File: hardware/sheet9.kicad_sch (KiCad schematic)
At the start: 0 parts

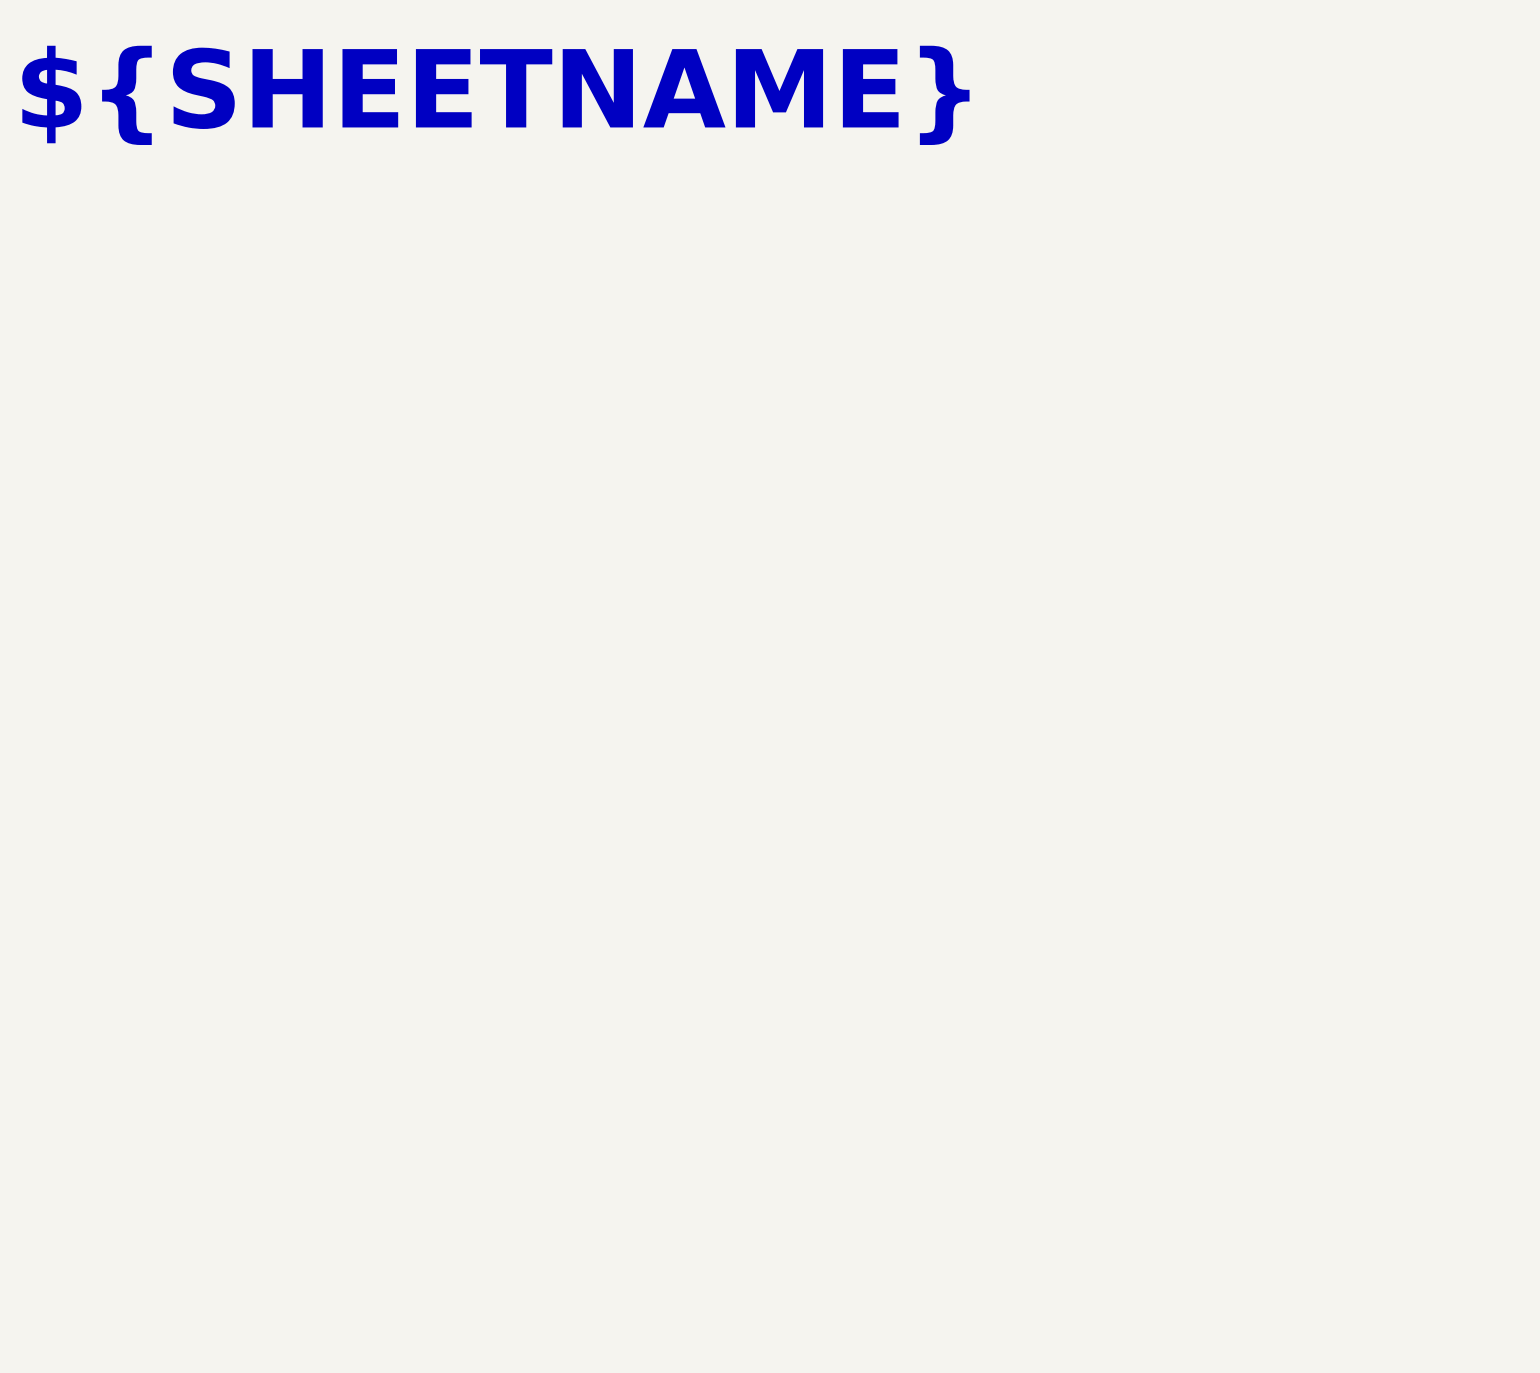
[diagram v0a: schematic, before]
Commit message: hardware(feat): add board layers
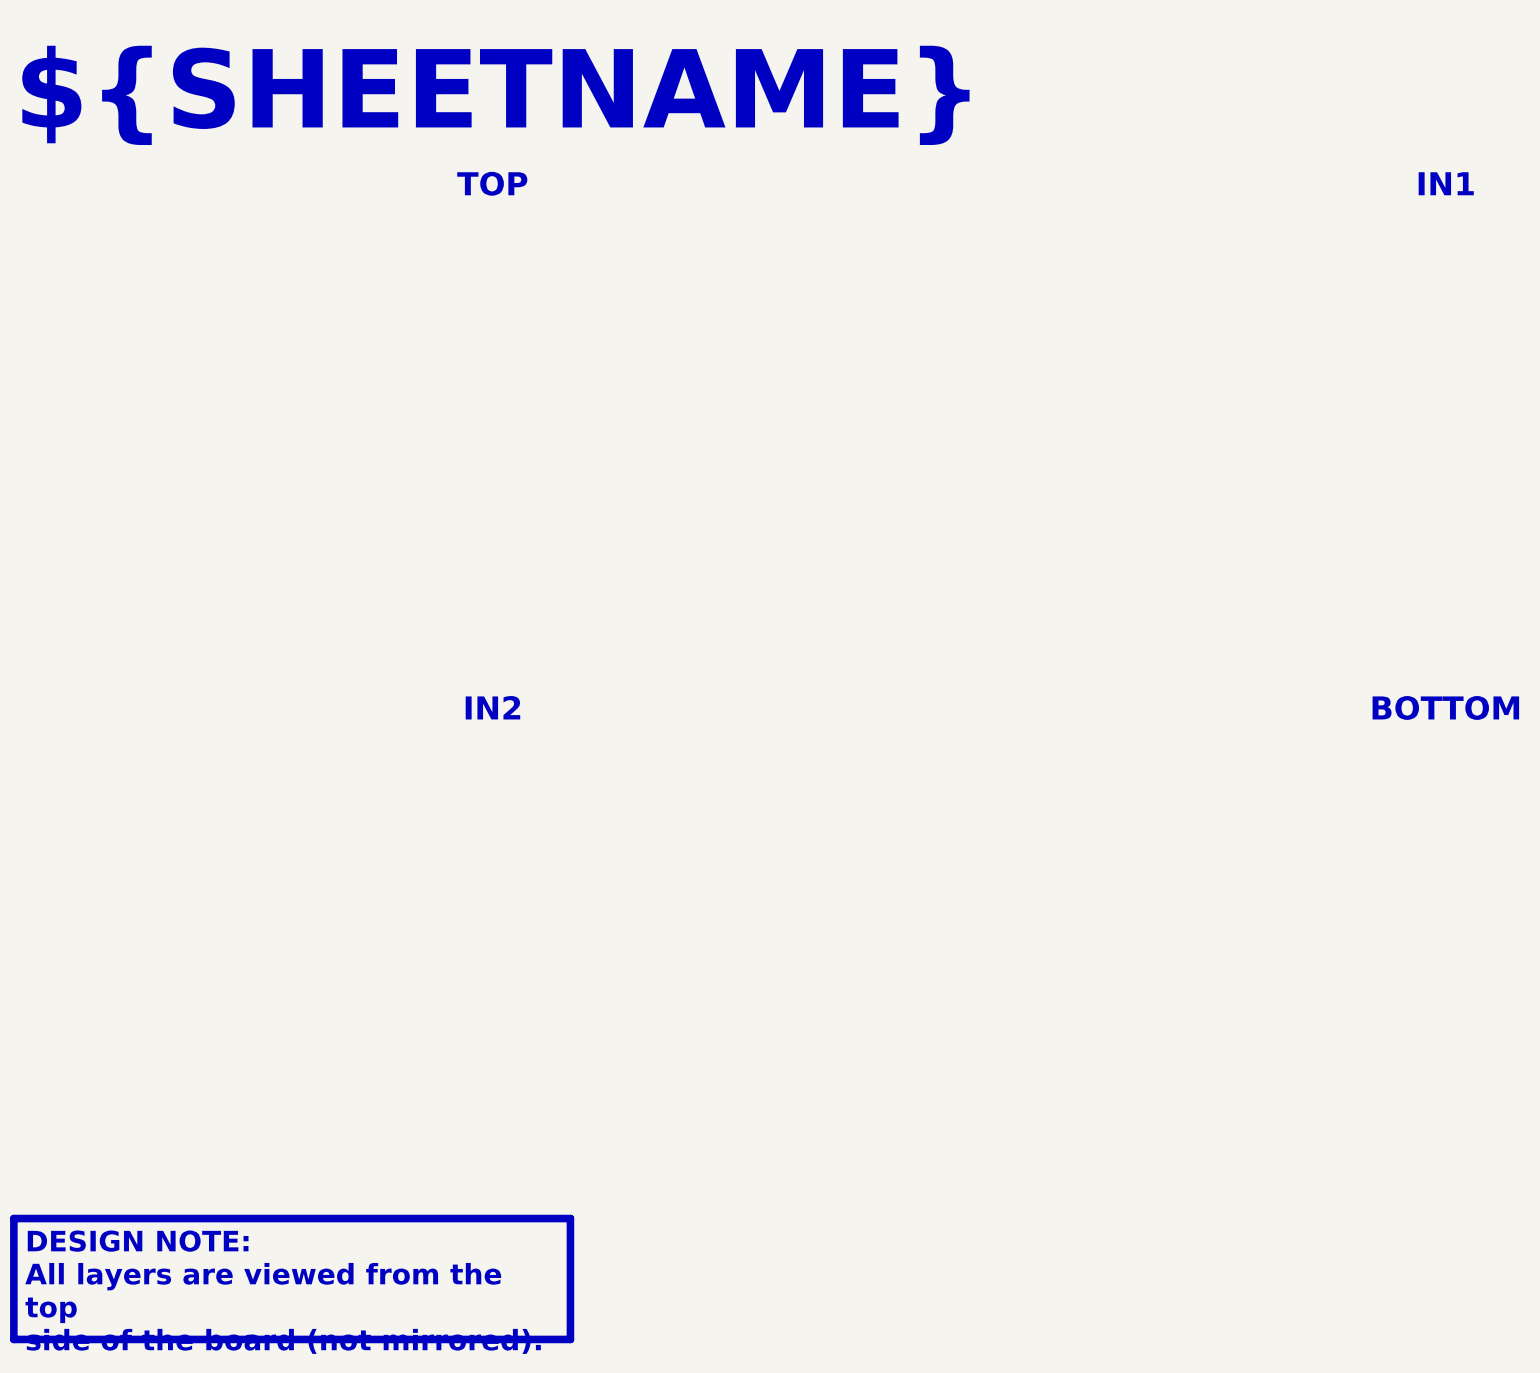
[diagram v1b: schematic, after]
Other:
- note added: "BOTTOM"
- note added: "IN1"
- note added: "IN2"
- note added: "TOP"
